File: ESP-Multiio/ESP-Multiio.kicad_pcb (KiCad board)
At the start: 2 copper layers, 74 x 59 mm, 40 parts, among them J1 Conn_01x10, SW1 SW_SPDT_MSM, SW2 SW_SPDT_MSM, SW3 SW_SPDT_MSM, SW4 SW_SPDT_MSM, U1 WeMos_D1_mini, U2 MCP23017_SP

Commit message: +IR
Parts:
- added C2: 100 nF, Capacitor_SMD:C_1206_3216Metric_Pad1.42x1.75mm_HandSolder, B.Cu at (134.1, 29.0)
- added D-IR1: LED, LED_THT:LED_D3.0mm, F.Cu at (127.6, 32.0)
- added Q1: BC337, Package_TO_SOT_THT:TO-92_Inline, B.Cu at (140.0, 34.0)
- added R10: 53 Ω, Resistor_SMD:R_1206_3216Metric_Pad1.42x1.75mm_HandSolder, B.Cu at (128.6, 35.5)
- added R11: 33 kΩ, Resistor_SMD:R_1206_3216Metric_Pad1.42x1.75mm_HandSolder, F.Cu at (140.1, 30.5)
- added R12: 100Ω, Resistor_SMD:R_1206_3216Metric_Pad1.42x1.75mm_HandSolder, B.Cu at (129.1, 29.0)
- added R9: 2.1kΩ, Resistor_SMD:R_1206_3216Metric_Pad1.42x1.75mm_HandSolder, F.Cu at (131.5, 48.0)
- added U4: TSOP1838, TSOP1838:TSOP18XX, F.Cu at (135.1, 32.0)
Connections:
- net Net-(R1-Pad2) renamed /GPA0
- net Net-(R2-Pad2) renamed /GPA1
- net Net-(R3-Pad2) renamed /GPA2
- net Net-(R4-Pad2) renamed /GPA3
- net Net-(R5-Pad2) renamed /GPA4
- net Net-(R6-Pad2) renamed /GPA5
- net Net-(R7-Pad2) renamed /GPA6
- net Net-(R8-Pad2) renamed /GPA7
- net Net-(SW1-Pad1) renamed /GPB1
- net Net-(SW1-Pad3) renamed /GPB0
- net Net-(SW2-Pad1) renamed /GPB3
- net Net-(SW2-Pad3) renamed /GPB2
- net Net-(SW3-Pad1) renamed /GPB5
- net Net-(SW3-Pad3) renamed /GPB4
- net Net-(SW4-Pad1) renamed /GPB7
- net Net-(SW4-Pad3) renamed /GPB6
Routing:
- net /D0: track 16.8 -> 95.4 mm
- net /D7: track 27.6 -> 48.6 mm, vias 0 -> 1
- net Net-(Q1-Pad2): track 0.00 -> 18.7 mm
- net Net-(C2-Pad1): track 0.00 -> 13.2 mm, vias 0 -> 1
- net Net-(Q1-Pad1): track 0.00 -> 10.5 mm
- net GND: track 11.2 -> 15.7 mm
- net Net-(D-IR1-Pad1): track 0.00 -> 3.69 mm

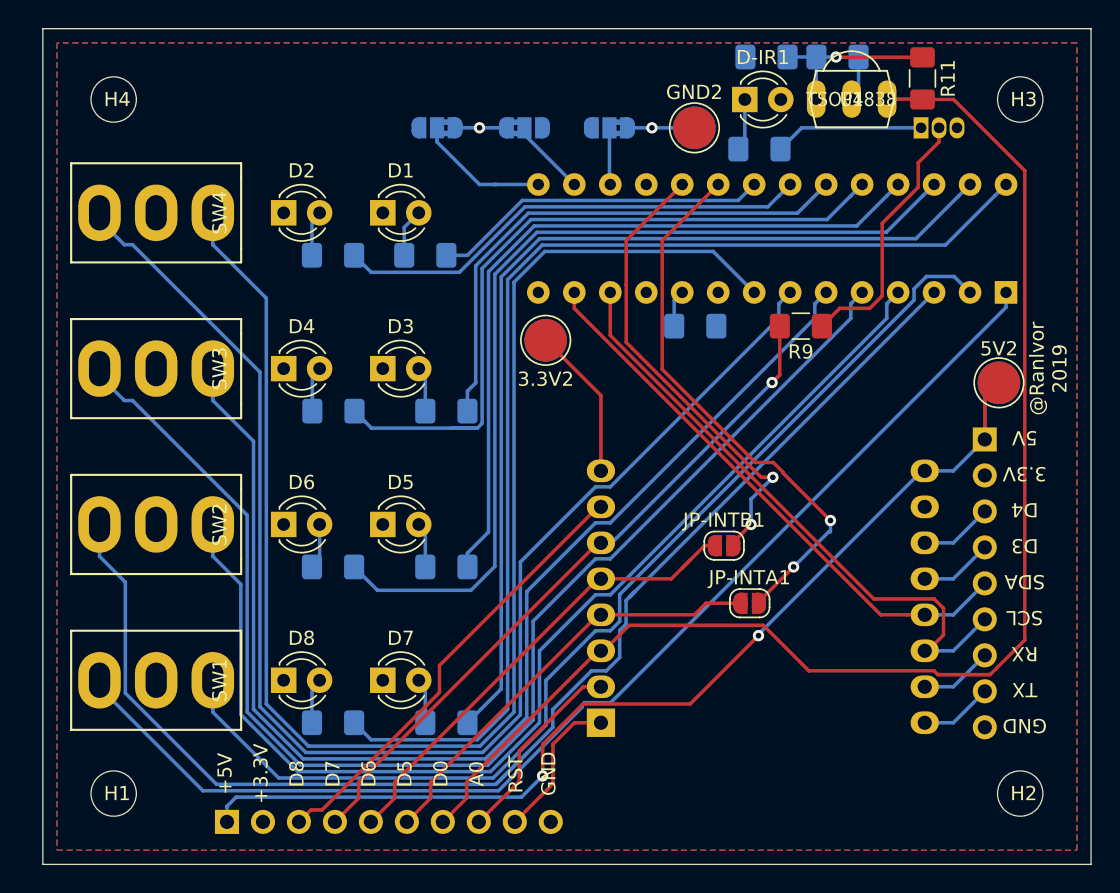
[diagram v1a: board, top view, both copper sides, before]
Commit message: Better switch-footprint, add twitter avatar, add github link
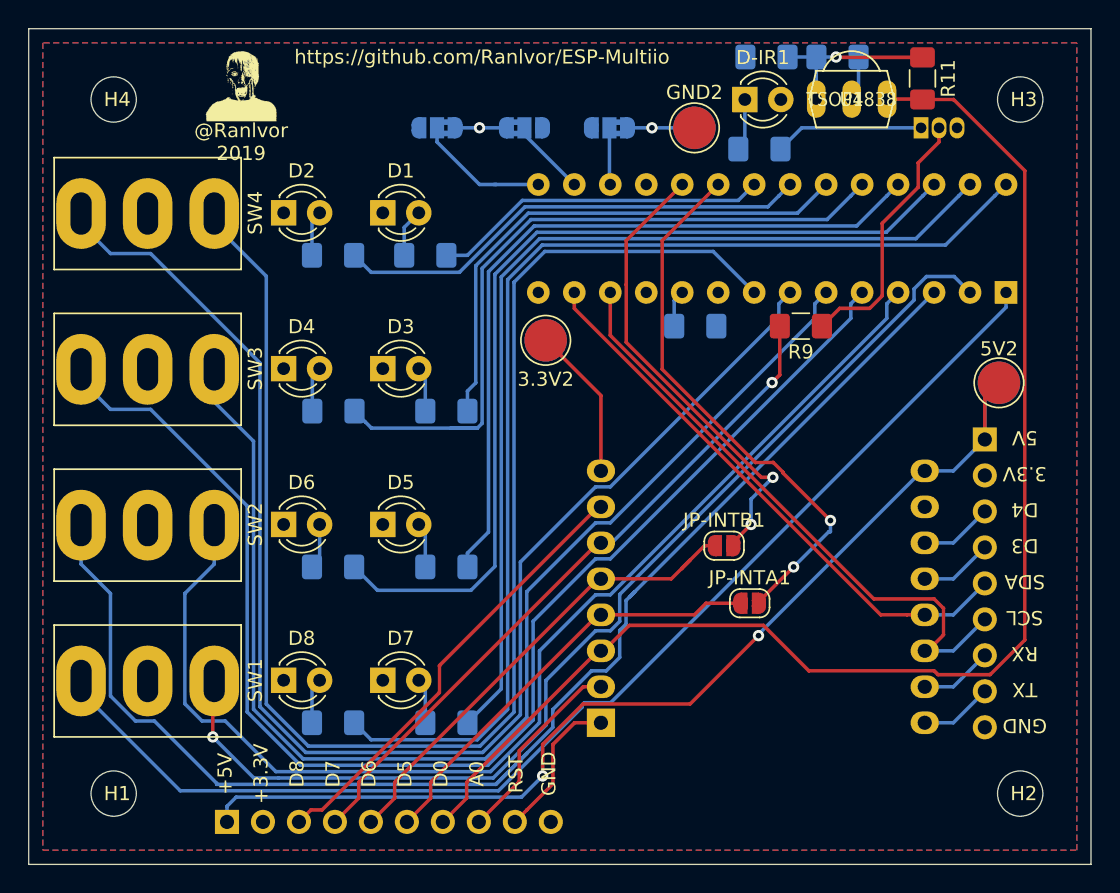
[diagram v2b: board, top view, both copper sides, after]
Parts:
- added G***: LOGO, logo:logo, B.Cu at (92.0, 31.0)
- added G***: LOGO, logo:logo, F.Cu at (92.0, 31.0)
- SW1, SW2, SW3, SW4: footprint Switch:Switch -> Switch:MTS-103
- moved SW1 4.47 mm to (92.0, 77.0)
- moved SW2 4.47 mm to (92.0, 66.0)
- moved SW3 4.47 mm to (92.0, 55.0)
- moved SW4 4.47 mm to (92.0, 44.0)
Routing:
- net /GPB3: track 79.9 -> 83.4 mm
- net /GPB5: track 86.6 -> 84.3 mm
- net /GPB6: track 99.5 -> 100.9 mm
- net /GPB1: track 78.5 -> 77.2 mm, vias 0 -> 1
- net /GPB4: track 93.4 -> 94.2 mm
- net /GPB2: track 93.7 -> 94.5 mm
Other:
- board size 74 x 59 mm -> 75 x 59 mm
- board text added: "https://github.com/Ranlvor/ESP-Multiio"
